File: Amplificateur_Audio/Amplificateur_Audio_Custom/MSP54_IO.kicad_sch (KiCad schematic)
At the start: 97 parts, among them J201 JTAG, J202 Conn_01x02, J203 Conn_02x08_Odd_Even, Q201 NPN, Q202 NPN, Q203 NPN, Q204 NPN, Q205 NPN, Q206 NPN, SW201 MUTE, SW202 VOL+, SW203 VOL-, SW204 MODE1, SW205 MODE2, SW206 MODE3, SW207 MODE4, SW208 LOAD, SW209 RESET, U201 MSP430F5234IRGZ, U202 TCA6408ARSVR, U203 24LC512, U204 TCA9548ARGER, Y201 32.768kHz

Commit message: Assignation des empreintes des composants de la première page
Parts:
- R201, R202, R203, R204, R205, R206, R207, R208, R209, R215, R216, R217, R218, R219, R220, R221, R222, R223, R224, R225, R226, R227, R228, R229, R233, R234, R235, R237, R238, R239, R240, R241, R242, R243, R244, R245, R246, R247, R248: footprint (none) -> 0402
- R210, R211, R212, R213, R214, R236: footprint (none) -> 0602
- R230, R231, R232: footprint (none) -> 0603
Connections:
- net P6.1: now also R221.2; no longer R224.2
- net P6.2: now also R222.2; no longer R226.2
- net P6.3: now also R226.2; no longer R223.2
- net P6.4: now also R224.2; no longer R222.2
- net P6.5: now also R223.2; no longer R221.2
- net at R226.1: now also Q204.2 (B); no longer Q205.2 (B)
- net at Q201.2 (B): now also R223.1; no longer R221.1
- net at D202.2 (A): now also R215.1; no longer R216.1
- net at R219.1: now also D204.2 (A); no longer D205.2 (A)
- net at Q202.2 (B): now also R221.1; no longer R224.1
- net at D201.2 (A): now also R217.1; no longer R215.1
- net at R218.1: now also D203.2 (A); no longer D204.2 (A)
- net at R222.1: now also Q205.2 (B); no longer Q203.2 (B)
- new net: D205.2 (A), R216.1
- new net: Q203.2 (B), R224.1
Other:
- moved on the sheet: C209, C210, C211, C212, C213, C214, C215, C216, C217, C219, C220, R227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

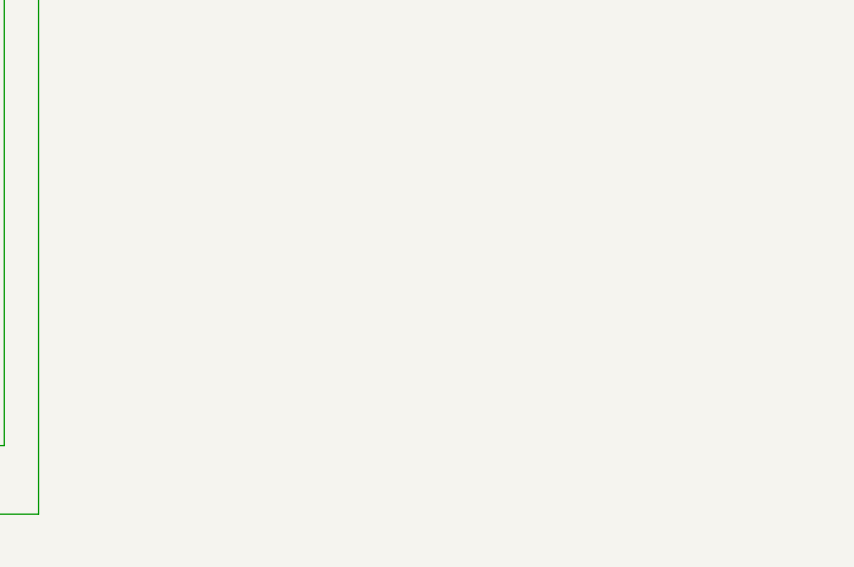
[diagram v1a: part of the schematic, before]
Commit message: Ajout de l'assignation des compostants et des empreintes jusqu'à la page 6
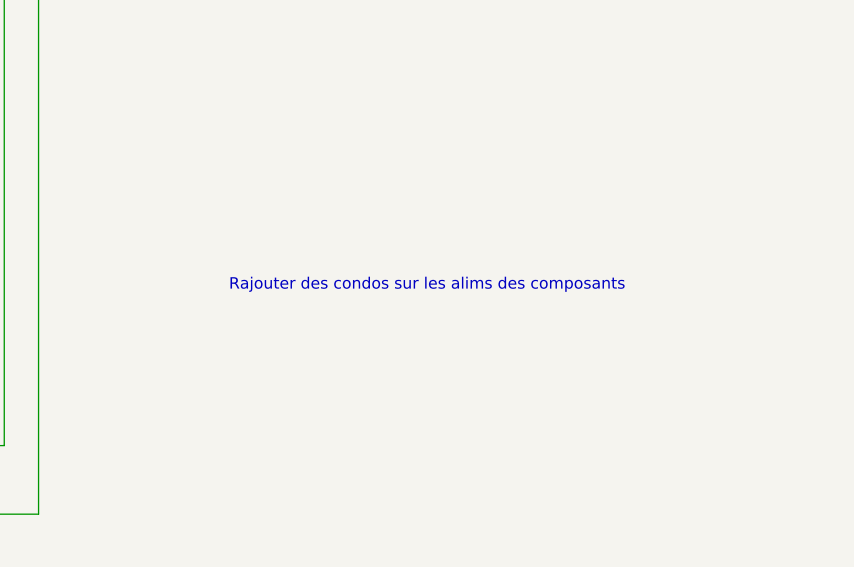
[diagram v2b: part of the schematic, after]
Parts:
- C201, C210: footprint 402 -> Capacitor_SMD:C_0402_1005Metric_Pad0.74x0.62mm_HandSolder
- C202, C204, C205, C206, C207, C208, C209, C211, C212, C213, C214, C215, C216, C219, C220: footprint 0402 -> Capacitor_SMD:C_0402_1005Metric_Pad0.74x0.62mm_HandSolder
- C203: footprint GRM1555C1E471JA01D -> Capacitor_SMD:C_0402_1005Metric_Pad0.74x0.62mm_HandSolder
- C217, C218: footprint 0603 -> Capacitor_SMD:C_0201_0603Metric_Pad0.64x0.40mm_HandSolder
- D201, D202, D203, D204, D205: footprint (none) -> LED_SMD:LED_0603_1608Metric_Pad1.05x0.95mm_HandSolder
- D206: footprint (none) -> LED_SMD:LED_0402_1005Metric_Pad0.77x0.64mm_HandSolder
- J201: footprint (none) -> PinSocket_1x06_P1.27mm_Vertical
- J202: footprint (none) -> PinHeader_1x02_P2.54mm_Vertical
- J203: footprint (none) -> PinHeader_2x08_P2.54mm_Vertical
- Q201, Q202, Q203, Q204, Q205, Q206: footprint (none) -> Package_TO_SOT_SMD:SOT-23
- R201, R202, R203, R204, R205, R206, R207, R208, R209, R215, R216, R217, R218, R219, R220, R221, R222, R223, R224, R225, R226, R227, R228, R229, R233, R234, R235, R237, R238, R239, R240, R241, R242, R243, R244, R245, R246, R247, R248: footprint 0402 -> Resistor_SMD:R_0402_1005Metric_Pad0.72x0.64mm_HandSolder
- R210, R211, R212, R213, R214, R236: footprint 0602 -> Resistor_SMD:R_0201_0603Metric_Pad0.64x0.40mm_HandSolder
- R230, R231, R232: footprint 0603 -> Resistor_SMD:R_0201_0603Metric_Pad0.64x0.40mm_HandSolder
- SW201, SW202, SW203, SW204, SW205, SW206, SW207, SW208, SW209: footprint (none) -> Button_Switch_SMD:SW_SPST_TL3342
- U203: footprint (none) -> Package_SO:TSSOP-8_4.4x3mm_P0.65mm
- Y201: footprint (none) -> Crystal:Crystal_SMD_3215-2Pin_3.2x1.5mm
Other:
- note added: "Rajouter des condos sur les alims des composants"

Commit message: Ajout de point de test et début du routage
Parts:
- added TP201: Mute, TestPoint:TestPoint_Pad_D1.5mm, symbol Connector:TestPoint
- added TP202, TP211: GND, TestPoint:TestPoint_Pad_D1.5mm, symbol Connector:TestPoint
- added TP203: VOL+, TestPoint:TestPoint_Pad_D1.5mm, symbol Connector:TestPoint
- added TP204: VOL-, TestPoint:TestPoint_Pad_D1.5mm, symbol Connector:TestPoint
- added TP205: MODE1, TestPoint:TestPoint_Pad_D1.5mm, symbol Connector:TestPoint
- added TP206: MODE2, TestPoint:TestPoint_Pad_D1.5mm, symbol Connector:TestPoint
- added TP207: MODE3, TestPoint:TestPoint_Pad_D1.5mm, symbol Connector:TestPoint
- added TP208: MODE4, TestPoint:TestPoint_Pad_D1.5mm, symbol Connector:TestPoint
- added TP209: LOAD, TestPoint:TestPoint_Pad_D1.5mm, symbol Connector:TestPoint
- added TP210: U203 AO, TestPoint:TestPoint_Pad_D1.5mm, symbol Connector:TestPoint
- added TP212: U203 VDD, TestPoint:TestPoint_Pad_D1.5mm, symbol Connector:TestPoint
- added TP213: WP, TestPoint:TestPoint_Pad_D1.5mm, symbol Connector:TestPoint
- added TP214: SCL, TestPoint:TestPoint_Pad_D1.5mm, symbol Connector:TestPoint
- added TP215: SDA, TestPoint:TestPoint_Pad_D1.5mm, symbol Connector:TestPoint
- added TP216: P5.5, TestPoint:TestPoint_Pad_D1.5mm, symbol Connector:TestPoint
- added TP217: P5.4, TestPoint:TestPoint_Pad_D1.5mm, symbol Connector:TestPoint
- added TP218: P6.0, TestPoint:TestPoint_Pad_D1.5mm, symbol Connector:TestPoint
- added TP219: P6.1, TestPoint:TestPoint_Pad_D1.5mm, symbol Connector:TestPoint
- added TP220: P6.2, TestPoint:TestPoint_Pad_D1.5mm, symbol Connector:TestPoint
- added TP221: P6.3, TestPoint:TestPoint_Pad_D1.5mm, symbol Connector:TestPoint
- added TP222: P6.4, TestPoint:TestPoint_Pad_D1.5mm, symbol Connector:TestPoint
- added TP223: P6.5, TestPoint:TestPoint_Pad_D1.5mm, symbol Connector:TestPoint
- added TP224: GND U201, TestPoint:TestPoint_Pad_D1.5mm, symbol Connector:TestPoint
- added TP225: RESET, TestPoint:TestPoint_Pad_D1.5mm, symbol Connector:TestPoint
- added TP226: AVCC U201, TestPoint:TestPoint_Pad_D1.5mm, symbol Connector:TestPoint
- added TP227: SBWTDIO, TestPoint:TestPoint_Pad_D1.5mm, symbol Connector:TestPoint
- added TP228: SBWTCK, TestPoint:TestPoint_Pad_D1.5mm, symbol Connector:TestPoint
- added TP229: /AMP-RESET1, TestPoint:TestPoint_Pad_D1.5mm, symbol Connector:TestPoint
- added TP230: /AMP-RESET2, TestPoint:TestPoint_Pad_D1.5mm, symbol Connector:TestPoint
- added TP231: /AMP-RESET3, TestPoint:TestPoint_Pad_D1.5mm, symbol Connector:TestPoint
- added TP232: /AMP-RESET4, TestPoint:TestPoint_Pad_D1.5mm, symbol Connector:TestPoint
- added TP233: /AMP-RESET5, TestPoint:TestPoint_Pad_D1.5mm, symbol Connector:TestPoint
- added TP234: VCC U202, TestPoint:TestPoint_Pad_D1.5mm, symbol Connector:TestPoint
- added TP235: RESET U202, TestPoint:TestPoint_Pad_D1.5mm, symbol Connector:TestPoint
- added TP236: GND U202, TestPoint:TestPoint_Pad_D1.5mm, symbol Connector:TestPoint
- added TP237: SDA1, TestPoint:TestPoint_Pad_D1.5mm, symbol Connector:TestPoint
- added TP238: SCL1, TestPoint:TestPoint_Pad_D1.5mm, symbol Connector:TestPoint
- added TP239: SDA2, TestPoint:TestPoint_Pad_D1.5mm, symbol Connector:TestPoint
- added TP240: SCL2, TestPoint:TestPoint_Pad_D1.5mm, symbol Connector:TestPoint
- added TP241: SDA3, TestPoint:TestPoint_Pad_D1.5mm, symbol Connector:TestPoint
- added TP242: SCL3, TestPoint:TestPoint_Pad_D1.5mm, symbol Connector:TestPoint
- added TP243: SDA4, TestPoint:TestPoint_Pad_D1.5mm, symbol Connector:TestPoint
- added TP244: SCL4, TestPoint:TestPoint_Pad_D1.5mm, symbol Connector:TestPoint
- added TP245: SDA5, TestPoint:TestPoint_Pad_D1.5mm, symbol Connector:TestPoint
- added TP246: SCL5, TestPoint:TestPoint_Pad_D1.5mm, symbol Connector:TestPoint
- added TP247: SDA6, TestPoint:TestPoint_Pad_D1.5mm, symbol Connector:TestPoint
- added TP248: SCL6, TestPoint:TestPoint_Pad_D1.5mm, symbol Connector:TestPoint
- added TP249: SDA U202, TestPoint:TestPoint_Pad_D1.5mm, symbol Connector:TestPoint
- added TP250: SCL U202, TestPoint:TestPoint_Pad_D1.5mm, symbol Connector:TestPoint
- added TP251: VCC U204, TestPoint:TestPoint_Pad_D1.5mm, symbol Connector:TestPoint
- added TP252: GDN U204, TestPoint:TestPoint_Pad_D1.5mm, symbol Connector:TestPoint
- added TP253: RESET U204, TestPoint:TestPoint_Pad_D1.5mm, symbol Connector:TestPoint
- added TP254: SCL U204, TestPoint:TestPoint_Pad_D1.5mm, symbol Connector:TestPoint
- added TP255: SDA U204, TestPoint:TestPoint_Pad_D1.5mm, symbol Connector:TestPoint
- J201: footprint PinSocket_1x06_P1.27mm_Vertical -> Connector_PinSocket_1.27mm:PinSocket_1x06_P1.27mm_Vertical
- J202: footprint PinHeader_1x02_P2.54mm_Vertical -> Connector_PinHeader_2.54mm:PinHeader_1x02_P2.54mm_Vertical
- J203: footprint PinHeader_2x08_P2.54mm_Vertical -> Connector_PinHeader_2.54mm:PinHeader_2x08_P2.54mm_Vertical
- U202: footprint TCA6408ARSVR:QFN40P180X260X55-16N -> NewLibrary:QFN40P180X260X55-16N
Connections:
- net 3.3V-3: now also TP234.1, TP251.1
- net 3V3: now also TP212.1, TP226.1
- net GND: now also TP202.1, TP211.1, TP224.1, TP236.1, TP252.1
- net P5.4: now also TP217.1
- net P5.5: now also TP216.1
- net P6.0: now also TP218.1
- net P6.1: now also TP219.1
- net P6.2: now also TP220.1
- net P6.3: now also TP221.1
- net P6.4: now also TP222.1
- net P6.5: now also TP223.1
- net SBWTCK: now also TP228.1
- net SBWTDIO: now also TP227.1
- net SCL: now also TP214.1, TP250.1, TP254.1; no longer J203.2 (Pin_2), R234.2, U201.22 (UCB0SIMO/UCB0SDA/P3.0), U202.13 (SDA), U203.5 (SDA), U204.20 (SDA)
- net SCL1: now also TP238.1
- net SCL2: now also TP240.1
- net SCL3: now also TP242.1
- net SCL4: now also TP244.1
- net SCL5: now also TP246.1
- net SCL6: now also TP248.1
- net SDA1: now also TP237.1
- net SDA2: now also TP239.1
- net SDA3: now also TP241.1
- net SDA4: now also TP243.1
- net SDA5: now also TP245.1
- net SDA6: now also TP247.1
- net /AMP-RESET1: now also TP229.1
- net /AMP-RESET2: now also TP230.1
- net /AMP-RESET3: now also TP231.1
- net /AMP-RESET4: now also TP232.1
- net /AMP-RESET5: now also TP233.1
- net /RESET: now also TP225.1
- net at C208.2, R208.1, SW208.2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: now also TP209.1
- net at C204.2, R204.1, SW204.2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: now also TP205.1
- net at R230.1, R231.2, U203.1 (A0): now also TP210.1
- net at R232.2, R233.2, U203.7 (WP): now also TP213.1
- net at C202.2, R202.1, SW202.2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: now also TP203.1
- net at C203.2, R203.1, SW203.2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: now also TP204.1
- net at C205.2, R205.1, SW205.2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: now also TP206.1
- net at C206.2, R206.1, SW206.2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: now also TP207.1
- net at C201.2, R201.1, SW201.2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: now also TP201.1
- net at C207.2, R207.1, SW207.2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: now also TP208.1
- net at R236.1, U204.24 (~{RESET}): now also TP253.1
- net at R209.1, U202.1 (~{RESET}): now also TP235.1
- new net SDA: J203.2 (Pin_2), R234.2, TP215.1, TP249.1, TP255.1, U201.22 (UCB0SIMO/UCB0SDA/P3.0), U202.13 (SDA), U203.5 (SDA), U204.20 (SDA)
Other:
- moved on the sheet: C209, C210, C211, C212, C213, C214, C215, C216, C217, C218, J201, J202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

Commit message: Refactor : hierarchical template channels for multichannel routing
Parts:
- C201, C202, C203, C204, C205, C206, C207, C208, C209, C210, C211, C212, C213, C214, C215, C216, C219, C220: footprint Capacitor_SMD:C_0402_1005Metric_Pad0.74x0.62mm_HandSolder -> Capacitor_SMD:C_0402_1005Metric
- C217, C218: footprint Capacitor_SMD:C_0201_0603Metric_Pad0.64x0.40mm_HandSolder -> Capacitor_SMD:C_0402_1005Metric
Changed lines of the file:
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@@
 			)
 		)
-		(property "Footprint" "Capacitor_SMD:C_0402_1005Metric_Pad0.74x0.62mm_HandSolder"
+		(property "Footprint" "Capacitor_SMD:C_0402_1005Metric"
 			(at 30.48 177.8 0)
 			(effects
@@
 			)
 		)
-		(property "Footprint" "Capacitor_SMD:C_0402_1005Metric_Pad0.74x0.62mm_HandSolder"
+		(property "Footprint" "Capacitor_SMD:C_0402_1005Metric"
 			(at 149.225 269.24 0)
 			(effects
@@
 			)
 		)
-		(property "Footprint" "Capacitor_SMD:C_0402_1005Metric_Pad0.74x0.62mm_HandSolder"
+		(property "Footprint" "Capacitor_SMD:C_0402_1005Metric"
 			(at 30.48 116.84 0)
 			(effects
@@
 			)
 		)
-		(property "Footprint" "Capacitor_SMD:C_0402_1005Metric_Pad0.74x0.62mm_HandSolder"
+		(property "Footprint" "Capacitor_SMD:C_0402_1005Metric"
 			(at 30.48 137.16 0)
 			(effects
@@
 			)
 		)
-		(property "Footprint" "Capacitor_SMD:C_0402_1005Metric_Pad0.74x0.62mm_HandSolder"
+		(property "Footprint" "Capacitor_SMD:C_0402_1005Metric"
 			(at 210.185 269.24 0)
 			(effects
@@
 			)
 		)
-		(property "Footprint" "Capacitor_SMD:C_0402_1005Metric_Pad0.74x0.62mm_HandSolder"
+		(property "Footprint" "Capacitor_SMD:C_0402_1005Metric"
 			(at 189.865 269.24 0)
 			(effects
@@
 			)
 		)
-		(property "Footprint" "Capacitor_SMD:C_0402_1005Metric_Pad0.74x0.62mm_HandSolder"
+		(property "Footprint" "Capacitor_SMD:C_0402_1005Metric"
 			(at 200.025 269.24 0)
 			(effects
@@
 			)
 		)
-		(property "Footprint" "Capacitor_SMD:C_0402_1005Metric_Pad0.74x0.62mm_HandSolder"
+		(property "Footprint" "Capacitor_SMD:C_0402_1005Metric"
 			(at 159.385 269.24 0)
 			(effects
@@
 			)
 		)
-		(property "Footprint" "Capacitor_SMD:C_0402_1005Metric_Pad0.74x0.62mm_HandSolder"
+		(property "Footprint" "Capacitor_SMD:C_0402_1005Metric"
 			(at 30.48 54.61 0)
 			(effects
@@
 			)
 		)
-		(property "Footprint" "Capacitor_SMD:C_0402_1005Metric_Pad0.74x0.62mm_HandSolder"
+		(property "Footprint" "Capacitor_SMD:C_0402_1005Metric"
 			(at 30.48 95.25 0)
 			(effects
@@
 			)
 		)
-		(property "Footprint" "Capacitor_SMD:C_0402_1005Metric_Pad0.74x0.62mm_HandSolder"
+		(property "Footprint" "Capacitor_SMD:C_0402_1005Metric"
 			(at 130.81 172.72 0)
 			(effects
@@
 			)
 		)
-		(property "Footprint" "Capacitor_SMD:C_0201_0603Metric_Pad0.64x0.40mm_HandSolder"
+		(property "Footprint" "Capacitor_SMD:C_0402_1005Metric"
 			(at 189.23 34.29 0)
 			(effects
@@
 			)
 		)
-		(property "Footprint" "Capacitor_SMD:C_0402_1005Metric_Pad0.74x0.62mm_HandSolder"
+		(property "Footprint" "Capacitor_SMD:C_0402_1005Metric"
 			(at 139.065 269.24 0)
 			(effects
@@
 			)
 		)
-		(property "Footprint" "Capacitor_SMD:C_0201_0603Metric_Pad0.64x0.40mm_HandSolder"
+		(property "Footprint" "Capacitor_SMD:C_0402_1005Metric"
 			(at 193.04 78.74 0)
 			(effects
@@
 			)
 		)
-		(property "Footprint" "Capacitor_SMD:C_0402_1005Metric_Pad0.74x0.62mm_HandSolder"
+		(property "Footprint" "Capacitor_SMD:C_0402_1005Metric"
 			(at 179.705 269.24 0)
 			(effects
@@
 			)
 		)
-		(property "Footprint" "Capacitor_SMD:C_0402_1005Metric_Pad0.74x0.62mm_HandSolder"
+		(property "Footprint" "Capacitor_SMD:C_0402_1005Metric"
 			(at 115.57 172.72 0)
 			(effects
@@
 			)
 		)
-		(property "Footprint" "Capacitor_SMD:C_0402_1005Metric_Pad0.74x0.62mm_HandSolder"
+		(property "Footprint" "Capacitor_SMD:C_0402_1005Metric"
 			(at 169.545 269.24 0)
 			(effects
@@
 			)
 		)
-		(property "Footprint" "Capacitor_SMD:C_0402_1005Metric_Pad0.74x0.62mm_HandSolder"
+		(property "Footprint" "Capacitor_SMD:C_0402_1005Metric"
 			(at 30.48 34.29 0)
 			(effects
@@
 			)
 		)
-		(property "Footprint" "Capacitor_SMD:C_0402_1005Metric_Pad0.74x0.62mm_HandSolder"
+		(property "Footprint" "Capacitor_SMD:C_0402_1005Metric"
 			(at 30.48 74.93 0)
 			(effects
@@
 			)
 		)
-		(property "Footprint" "Capacitor_SMD:C_0402_1005Metric_Pad0.74x0.62mm_HandSolder"
+		(property "Footprint" "Capacitor_SMD:C_0402_1005Metric"
 			(at 30.48 157.48 0)
 			(effects
